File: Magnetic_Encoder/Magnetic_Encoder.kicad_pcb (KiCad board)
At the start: 2 copper layers, 2 parts, among them J1 Conn_01x04, U1 TLV493D-A1B6

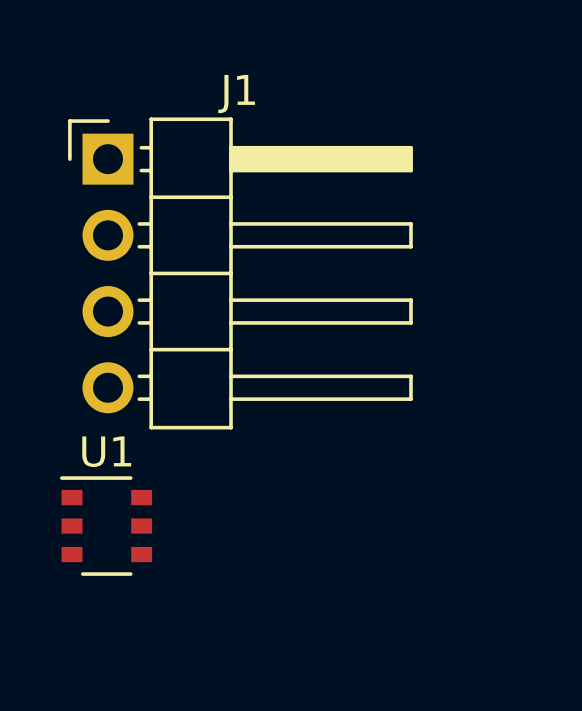
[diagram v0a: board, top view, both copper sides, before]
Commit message: Finalized compact magnetic encoder design
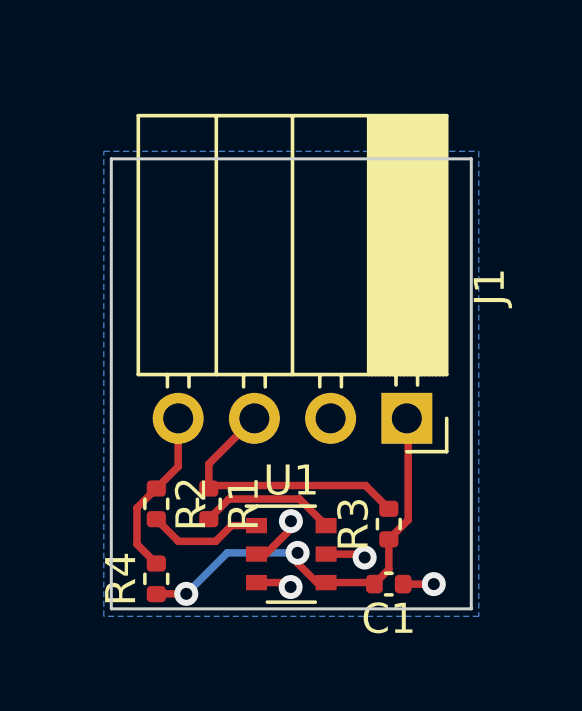
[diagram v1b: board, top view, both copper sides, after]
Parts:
- added C1: 0.1uF, Capacitor_SMD:C_0402_1005Metric, F.Cu at (29.2, 34.2)
- added R1: 100, Resistor_SMD:R_0402_1005Metric, F.Cu at (23.2, 31.5)
- added R2: 100, Resistor_SMD:R_0402_1005Metric, F.Cu at (21.5, 31.5)
- added R3: 1.2K, Resistor_SMD:R_0402_1005Metric, F.Cu at (29.2, 32.2)
- added R4: 1.2K, Resistor_SMD:R_0402_1005Metric, F.Cu at (21.5, 34.0)
- J1: footprint Connector_PinHeader_2.54mm:PinHeader_1x04_P2.54mm_Horizontal -> Connector_PinSocket_2.54mm:PinSocket_1x04_P2.54mm_Horizontal
- moved J1 13.2 mm to (29.9, 28.6), turned to -90 degrees
- moved U1 6.22 mm to (26.0, 33.2)
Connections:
- U1 pad 1: /SCL -> Net-(U1-SCL)
- U1 pad 6: /SDA -> Net-(U1-SDA)
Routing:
- net /VCC: track 0.00 -> 14.5 mm, vias 0 -> 2
- net /SDA: track 0.00 -> 9.33 mm
- net /SCL: track 0.00 -> 5.68 mm
- net GND: track 0.00 -> 5.30 mm, vias 0 -> 4
- net Net-(U1-SDA): track 0.00 -> 4.55 mm
- net Net-(U1-SCL): track 0.00 -> 3.86 mm
- added copper zone on B.Cu, net GND
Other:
- board outline added: 12 x 15 mm

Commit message: Fixed some silkscreen stuff, started DRIFT bus layout
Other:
- board text added: "3.3V"
- board text added: "GND"
- board text added: "SCL"
- board text added: "SDA"
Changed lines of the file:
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@@
   (gr_rect (start 20 20) (end 32 35)
     (stroke (width 0.1) (type default)) (fill none) (layer "Edge.Cuts"))
+  (gr_text "GND" (at 27.9 24.2 90) (layer "B.SilkS")
+    (effects (font (size 1 1) (thickness 0.15)) (justify left bottom mirror))
+  )
+  (gr_text "SDA" (at 25.4 24.3 90) (layer "B.SilkS")
+    (effects (font (size 1 1) (thickness 0.15)) (justify left bottom mirror))
+  )
+  (gr_text "SCL" (at 22.8 24.4 90) (layer "B.SilkS")
+    (effects (font (size 1 1) (thickness 0.15)) (justify left bottom mirror))
+  )
+  (gr_text "3.3V" (at 30.5 24 90) (layer "B.SilkS")
+    (effects (font (size 1 1) (thickness 0.15)) (justify left bottom mirror))
+  )
   (segment (start 26.2105 33.134098) (end 26.2105 33.4805) (width 0.25) (layer "F.Cu") (net 1))
   (segment (start 26.855 34.125) (end 27.16 34.125) (width 0.25) (layer "F.Cu") (net 1))
